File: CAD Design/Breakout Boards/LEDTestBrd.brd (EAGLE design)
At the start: 22.5 x 22.9 mm, 14 parts

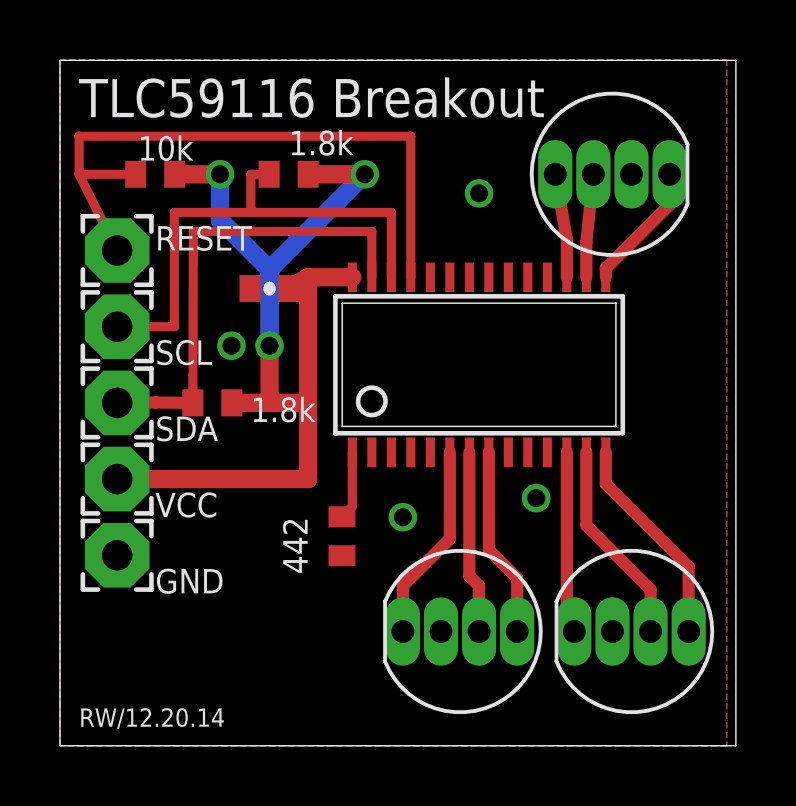
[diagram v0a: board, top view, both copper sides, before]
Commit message: First breakout board design review
Minor changes to silkscreens, added documentation.  Acc. and LED driver
boards ready for board house.
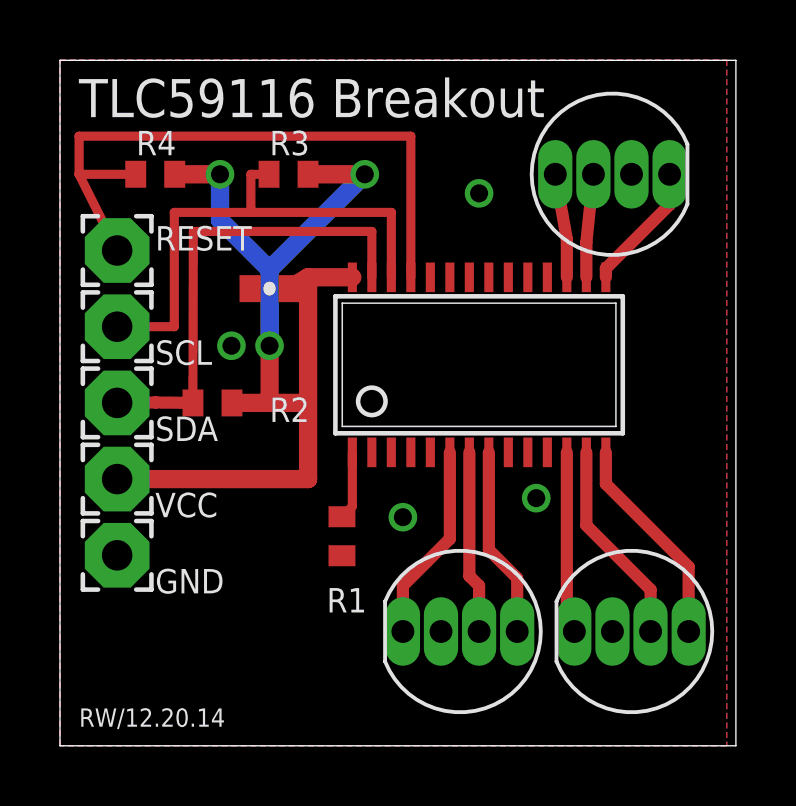
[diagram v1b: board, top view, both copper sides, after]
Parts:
- R4: value 10k -> 1.8k
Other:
- board text added: "R1"
- board text added: "R2"
- board text added: "R3"
- board text added: "R4"
- board text removed: "1.8k"
- board text removed: "10k"
- board text removed: "442"
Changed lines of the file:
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@@
 <text x="3.175" y="10.16" size="0.8128" layer="25">SDA</text>
 <text x="3.175" y="16.51" size="0.8128" layer="25">RESET</text>
-<text x="7.62" y="19.685" size="0.8128" layer="25">1.8k</text>
-<text x="6.35" y="10.795" size="0.8128" layer="25">1.8k</text>
-<text x="8.255" y="5.715" size="0.8128" layer="25" rot="R90">442</text>
-<text x="4.445" y="20.32" size="0.8128" layer="25" rot="R180">10k</text>
 <text x="0.635" y="20.955" size="1.27" layer="25">TLC59116 Breakout</text>
+<text x="8.89" y="4.445" size="0.8128" layer="25">R1</text>
+<text x="6.985" y="10.795" size="0.8128" layer="25">R2</text>
+<text x="6.985" y="19.685" size="0.8128" layer="25">R3</text>
+<text x="2.54" y="19.685" size="0.8128" layer="25">R4</text>
 </plain>
 <attributes>
@@
 <attribute name="VALUE" x="1.905" y="7.35" size="0.0254" layer="27"/>
 </element>
-<element name="R4" library="resistor" package="R0402" value="10k" x="3.175" y="19.05" smashed="yes"/>
+<element name="R4" library="resistor" package="R0402" value="1.8k" x="3.175" y="19.05" smashed="yes"/>
 </elements>
 <signals>
